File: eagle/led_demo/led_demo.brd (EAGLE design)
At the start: 40.6 x 51.7 mm, 37 parts

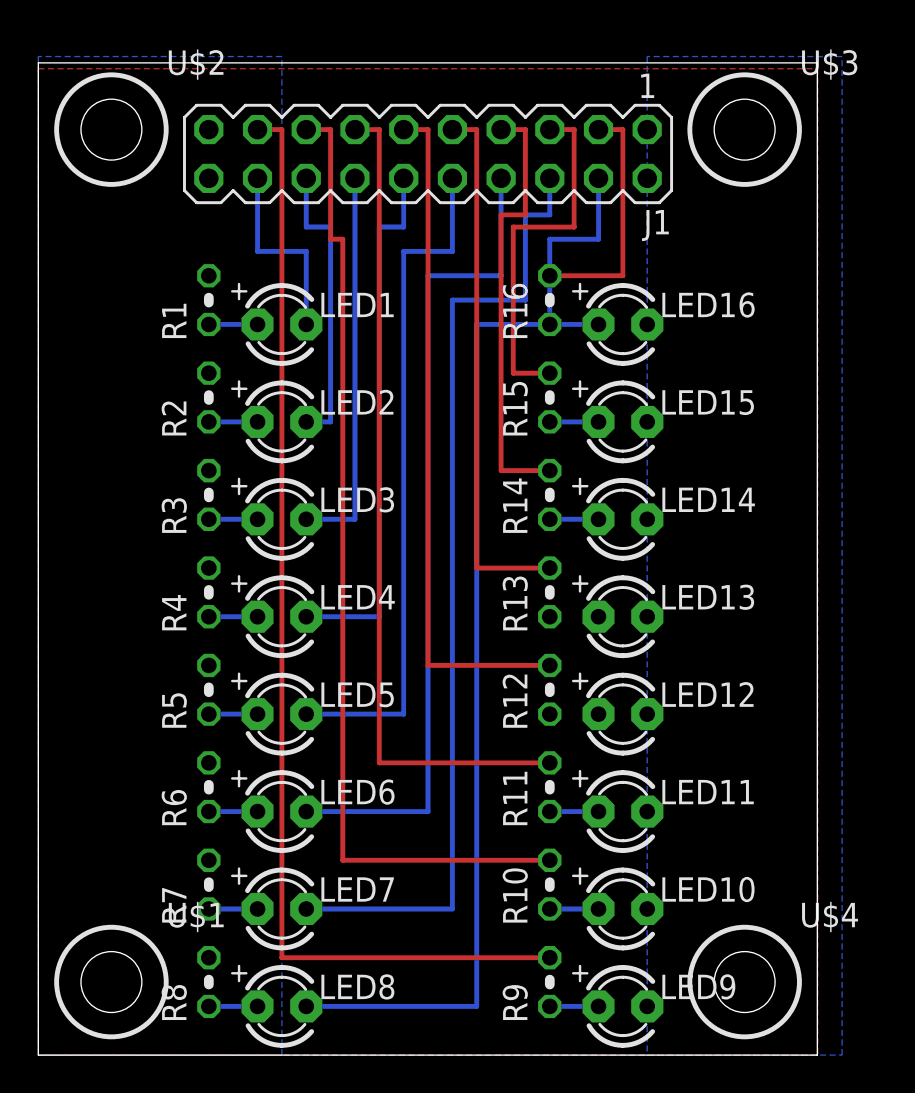
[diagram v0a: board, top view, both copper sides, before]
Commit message: changed trace width and isolate thickness to correct for missing traces on A406
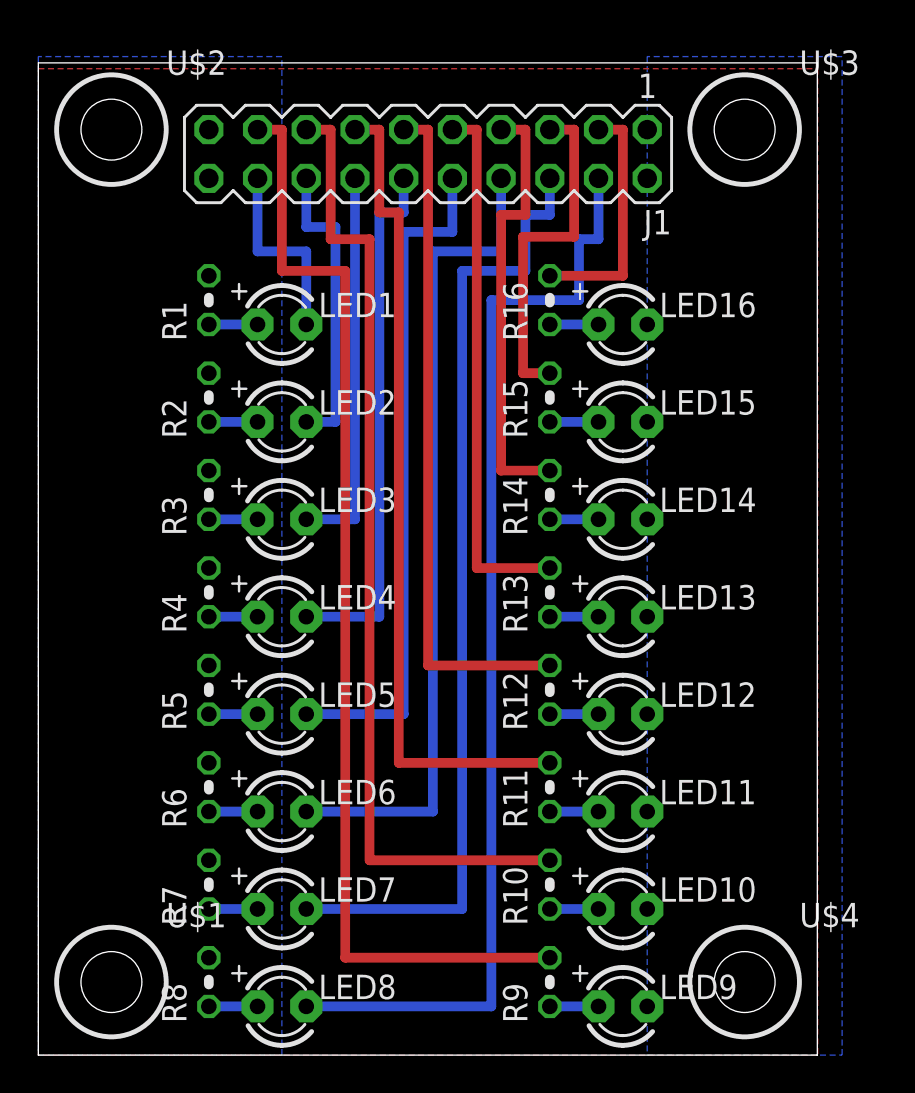
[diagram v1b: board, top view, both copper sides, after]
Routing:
- net N$21: track 0.00 -> 2.54 mm
- net N$20: track 0.00 -> 2.54 mm
- net N5: track 19.0 -> 18.0 mm
- net N16: track 15.2 -> 15.7 mm
